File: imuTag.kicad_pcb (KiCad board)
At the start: 4 copper layers, 30 x 30 mm, 36 parts, among them J1 Conn_ARM_SWD_TagConnect_TC203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, U1 E73-2G4M08S1C, U2 MX25R6435FZAIL0, U4 LSM6DSV16XTR, U5 LIS2MDLTR, Y2 Crystal

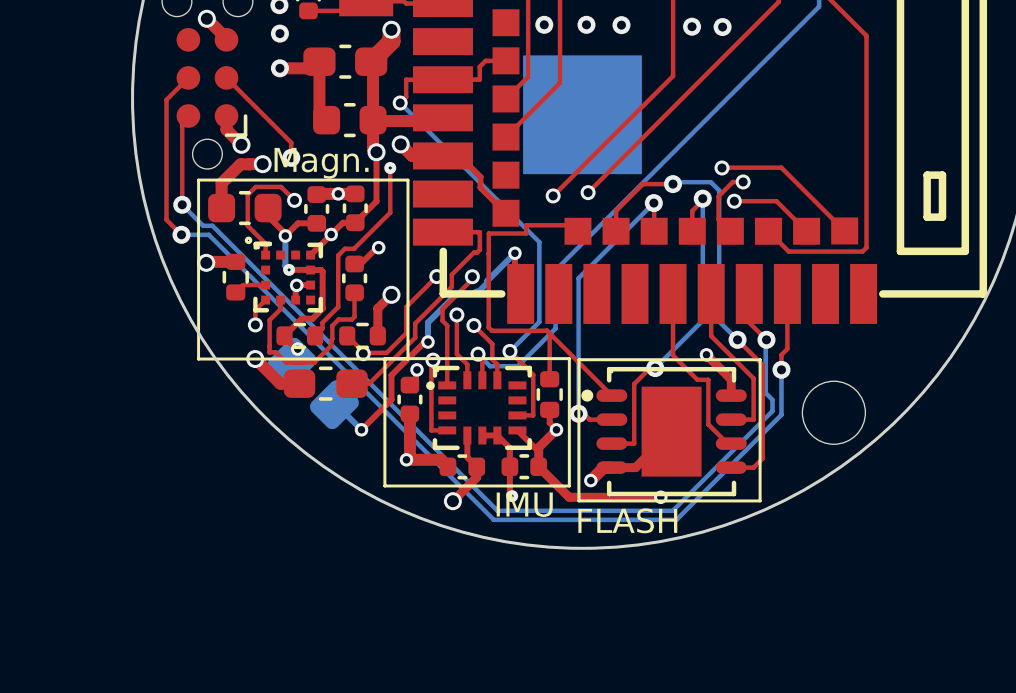
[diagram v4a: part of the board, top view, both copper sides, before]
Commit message: fix: minor wiring corrections under v1.2
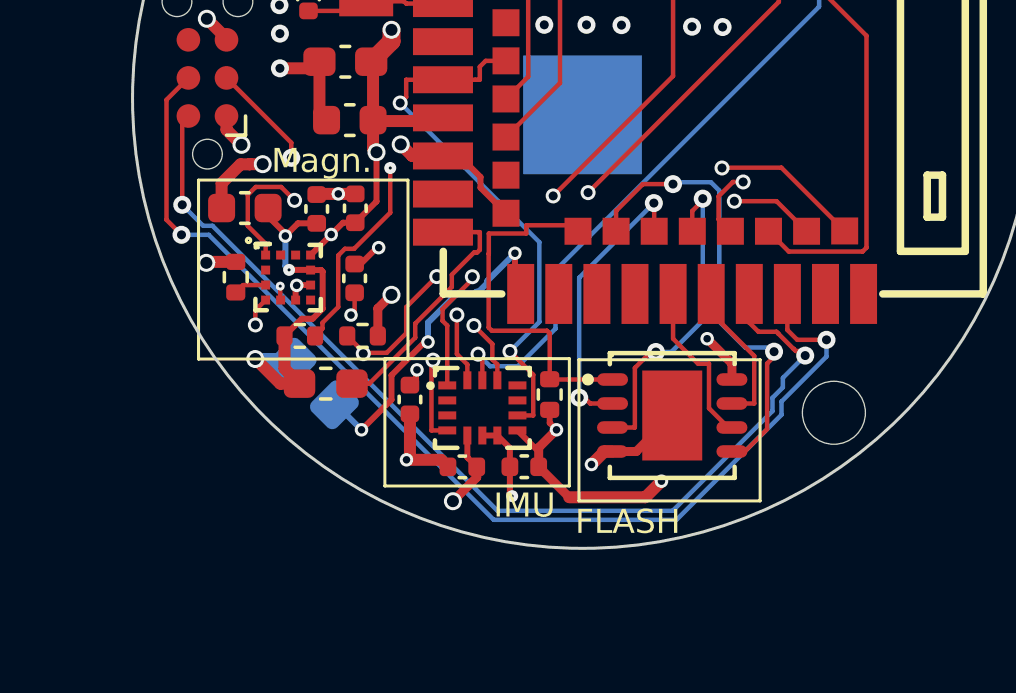
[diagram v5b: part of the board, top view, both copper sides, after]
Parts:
- moved U2 0.54 mm to (120.9, 111.0)
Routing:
- net VCC: track 45.7 -> 48.3 mm, vias 19 -> 18
- net Net-(U5-C1): track 6.67 -> 4.06 mm, vias 0 -> 2
- net /SWDIO: track 33.5 -> 35.8 mm
- net /SWDCLK: track 35.2 -> 36.9 mm
- net /QSPI_CS: track 13.2 -> 12.2 mm
- net /QSPI_IO1: track 10.2 -> 9.65 mm
- net /QSPI_CLK: track 6.08 -> 5.55 mm
- net /QSPI_IO3: track 5.77 -> 5.24 mm

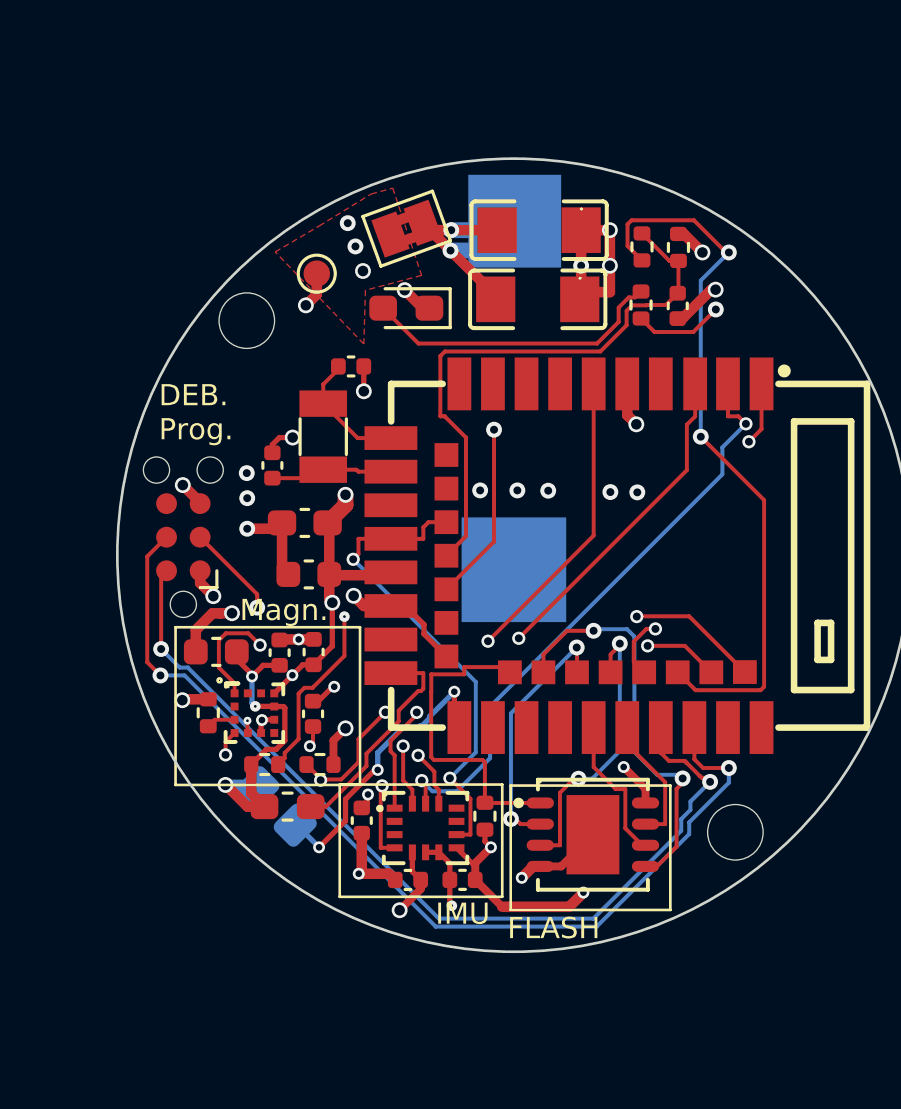
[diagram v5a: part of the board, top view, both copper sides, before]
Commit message: fix: wire unconnected pin and clear DRC exclusions
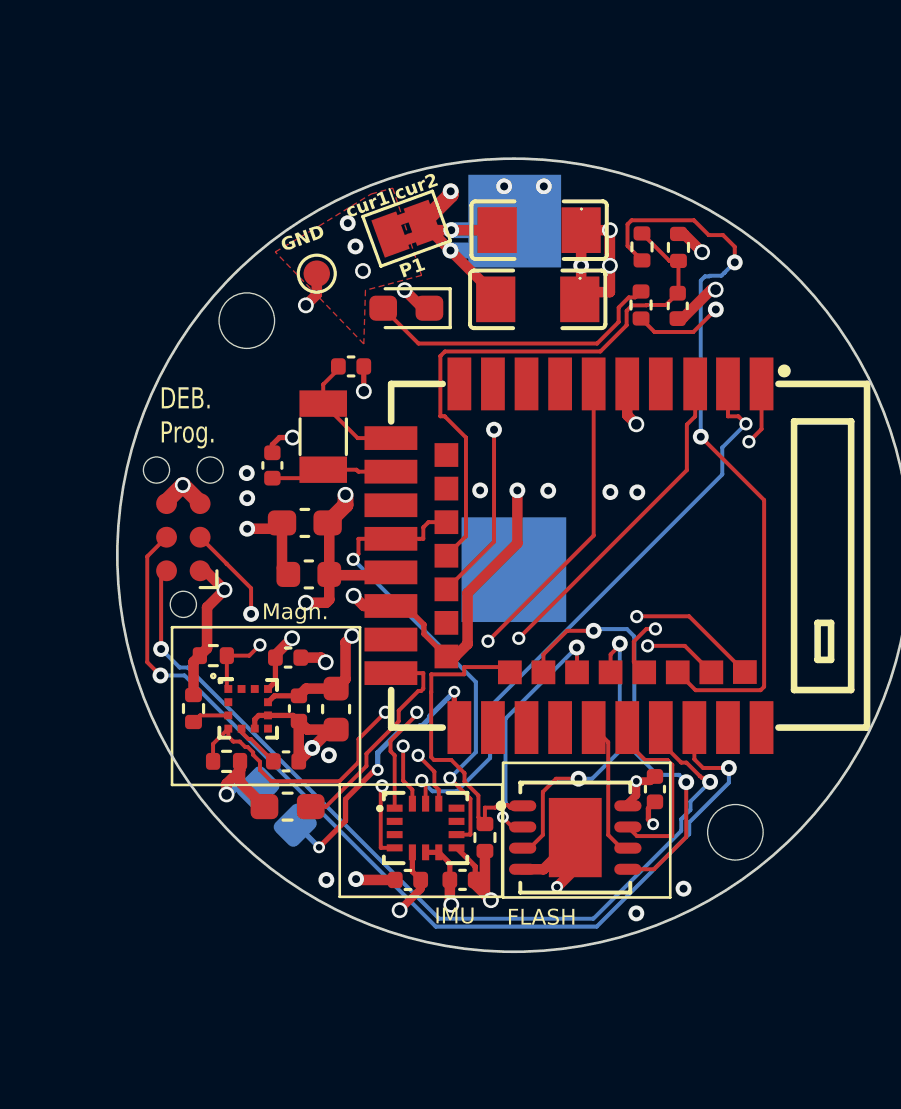
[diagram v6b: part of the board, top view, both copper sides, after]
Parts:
- moved C14 11.2 mm to (123.2, 109.3)
- moved C21 5.02 mm to (111.1, 106.3), turned to 90 degrees
- moved R16 4.56 mm to (106.5, 104.2)
- moved R18 3.54 mm to (107.0, 108.2)
- moved C19 2.24 mm to (109.7, 106.2), turned to 90 degrees
- moved C16 2.07 mm to (109.2, 108.2), turned to 180 degrees
- moved C17 0.99 mm to (109.3, 104.3), turned to 180 degrees
- moved R11 0.81 mm to (116.8, 111.1)
- moved U2 0.68 mm to (120.2, 111.1)
- moved R15 0.58 mm to (105.8, 106.2)
- moved U5 0.29 mm to (107.8, 106.3)
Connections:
- J1 pad 6: unconnected-(J1-SWO-Pad6) -> GND
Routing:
- net VCC: track 48.3 -> 36.3 mm, vias 18 -> 13
- net GND: track 39.6 -> 51.2 mm, vias 26 -> 29
- net /SPI1_MOSI: track 34.7 -> 26.3 mm
- net /I2C0_SCL: track 30.6 -> 22.4 mm, vias 3 -> 2
- net /QSPI_IO3: track 5.24 -> 7.76 mm
- net Net-(U5-C1): track 4.06 -> 1.79 mm, vias 2 -> 0
- net /SWDIO: track 35.8 -> 33.7 mm
- net /VBAT: track 14.3 -> 15.9 mm, vias 2 -> 5
- net /QSPI_IO0: track 15.4 -> 16.2 mm
- net /GPIO_BAT_MEAS: track 27.5 -> 28.2 mm
- net /QSPI_IO2: track 10.9 -> 11.4 mm
- net /I2C0_SDA: track 24.7 -> 25.2 mm, vias 4 -> 2
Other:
- board text added: "Battery-Type: C2032"
- board text added: "Bauer Labs IMU-TAG-Mini: A-1.0"
- board text added: "GND"
- board text added: "P1"
- board text added: "P1 current cut P1 and apply Probe Measurement to cur1 and cur2 ext.Power Apply Power-Supply to Supply GND and P1"
- board text added: "Prog. Interface GND GND SWDCLK RESET SWDIO VCC"
- board text added: "cur1|cur2"
- board text removed: "Bauer Labs IMU-TAG: A-1.0"
- board text removed: "C2032"

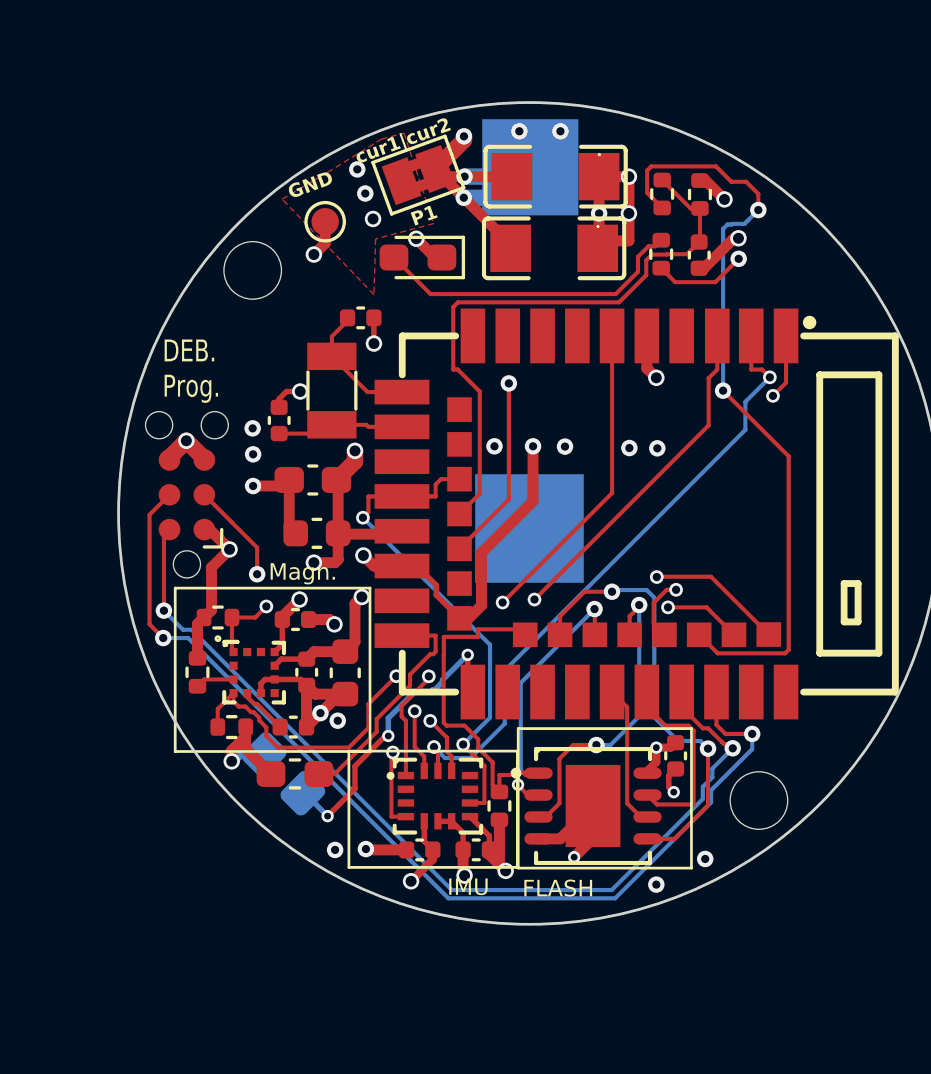
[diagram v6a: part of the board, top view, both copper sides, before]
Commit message: feat: optimize LIS2MDL layout for magnetic integrity
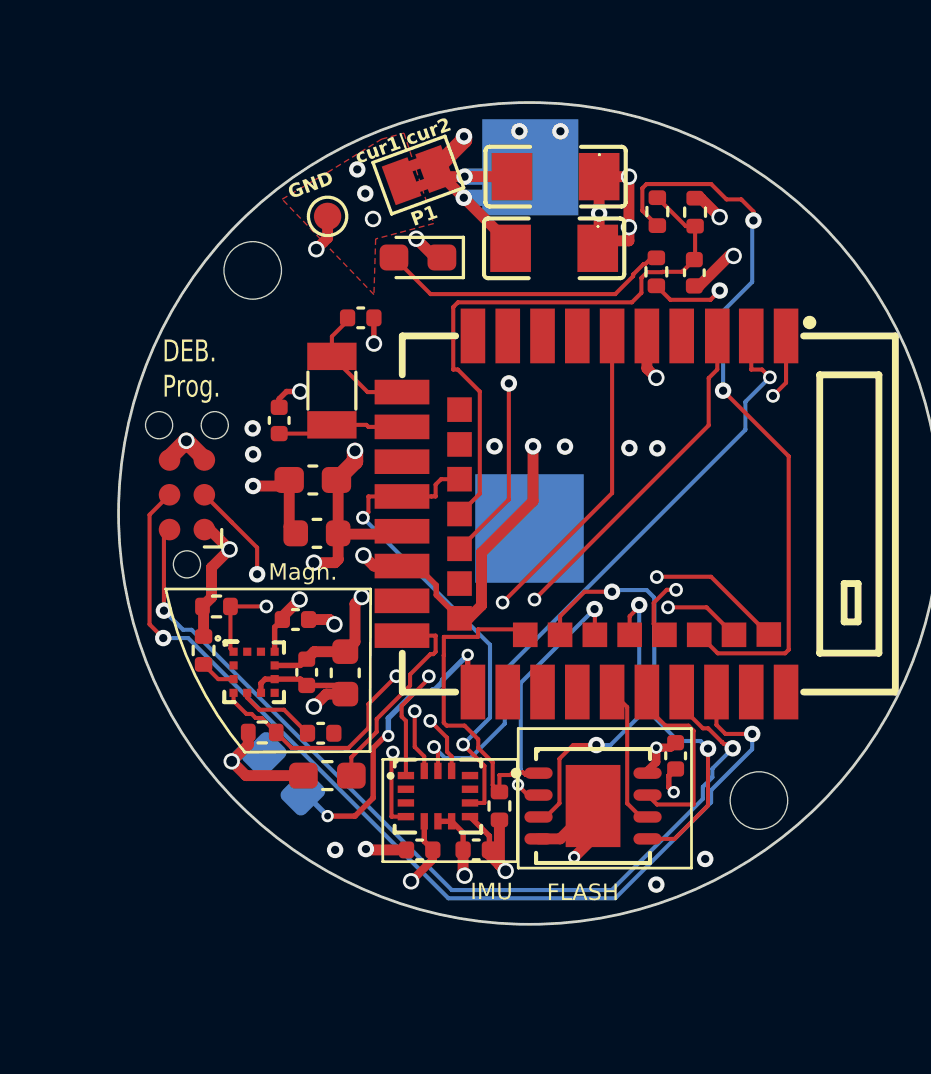
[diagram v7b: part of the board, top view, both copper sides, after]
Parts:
- moved L1 1.18 mm to (110.5, 110.0)
- moved R18 1.13 mm to (108.1, 108.4), turned to 0 degrees
- moved C16 1.02 mm to (110.2, 108.5)
- moved R15 0.83 mm to (106.0, 105.5)
- moved R3 0.67 mm to (122.5, 89.4)
- moved R2 0.67 mm to (123.9, 89.5)
- moved R5 0.67 mm to (122.5, 91.6)
- moved C1 0.67 mm to (123.9, 91.7)
- moved R16 0.41 mm to (106.4, 103.8)
- moved TP1 0.21 mm to (110.5, 89.6)
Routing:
- net GND: track 51.2 -> 49.1 mm, vias 29 -> 28
- net /LED1: track 20.4 -> 18.5 mm
- net /I2C0_SDA: track 25.2 -> 23.4 mm
- net Net-(U5-C1): track 1.79 -> 2.90 mm
- net /GPIO_BAT_MEAS: track 28.2 -> 27.2 mm
- net Net-(U1-DCH): track 8.44 -> 7.67 mm
- net Net-(D2-A): track 11.4 -> 10.7 mm
- net /RESET: track 26.4 -> 26.9 mm

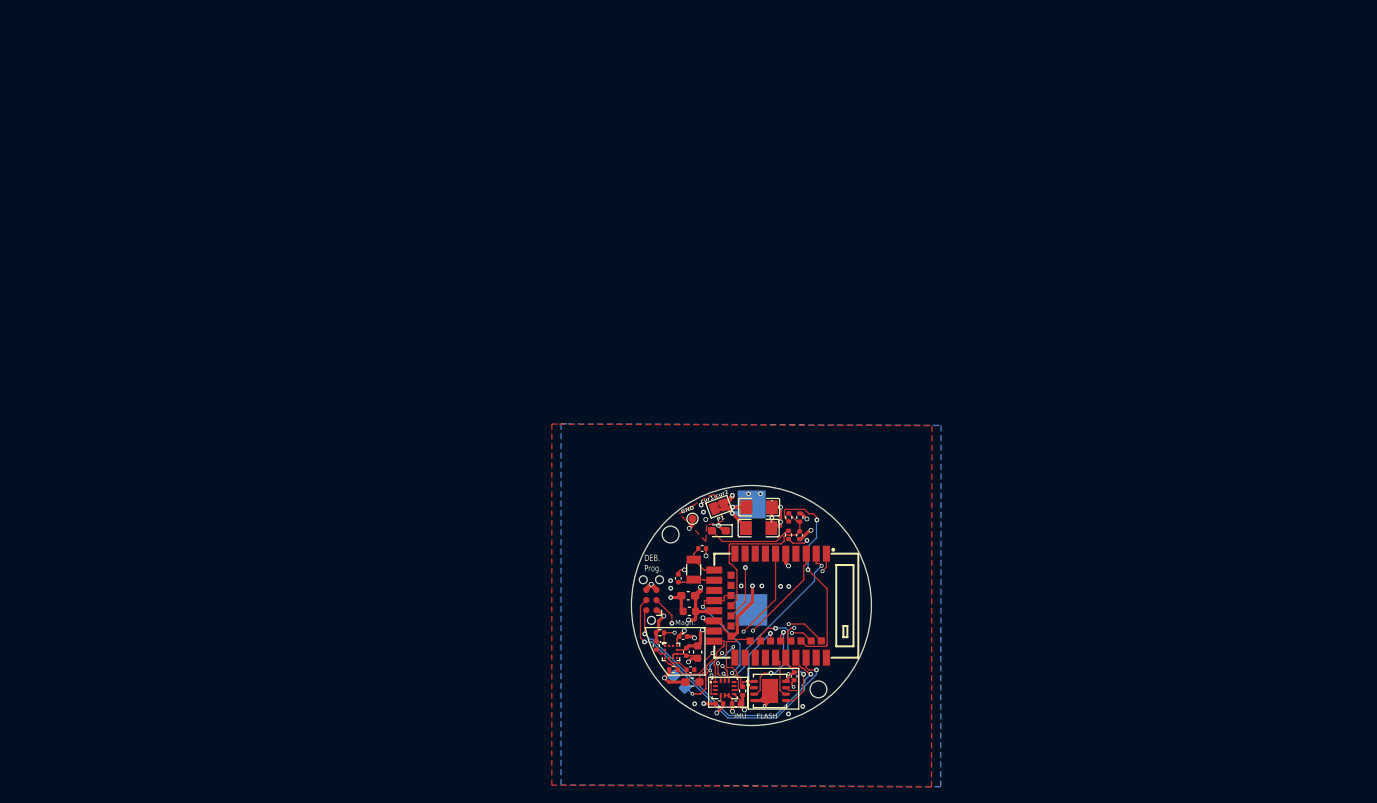
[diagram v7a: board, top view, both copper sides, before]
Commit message: feat: add NFC antenna support via E73-2G4M08S1C
- Add NFC matching network (ESD protection, 100pF tuning caps)
- Add hybrid antenna connector (JST SH 1.0mm + hand-solder test pads)
- Add 4-layer keepout zones around NFC traces and antenna feed
- Route and length-balance NFC1/NFC2 traces
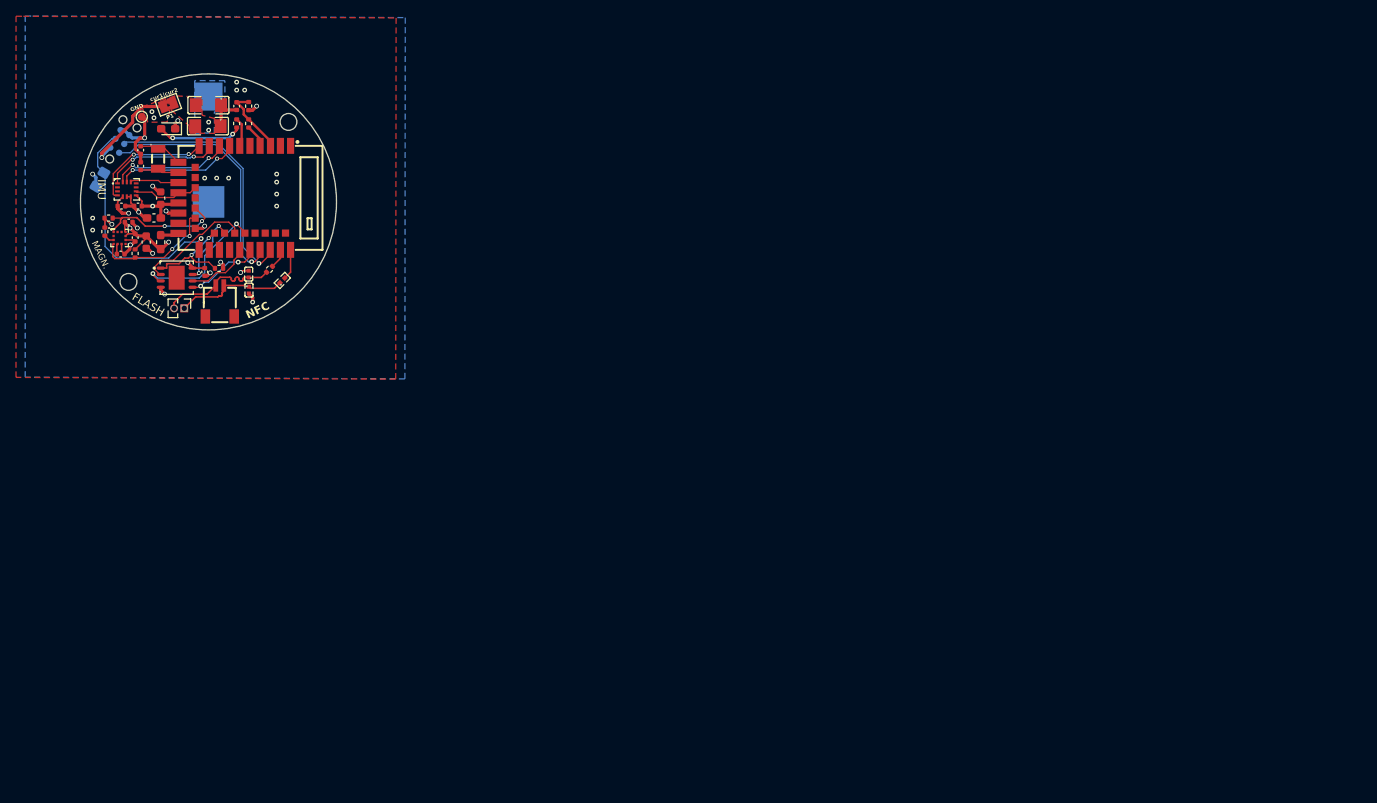
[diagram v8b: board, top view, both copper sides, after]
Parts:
- removed Y2: Crystal, Crystal:Crystal_SMD_3215-2Pin_3.2x1.5mm
- added C10: CC0402GRNPO9BN560, EasyEDA:C0402, F.Cu at (55.1, 61.0)
- added C9: CC0402GRNPO9BN560, EasyEDA:C0402, F.Cu at (55.0, 59.0)
- added CN1: SM02B-SRSS-TB, EasyEDA:CONN-SMD_2P-P1.00_SM02B-SRSS-TB-LF-SN, F.Cu at (51.4, 62.4)
- added J2: Conn_01x02_Pin, Connector_PinHeader_1.27mm:PinHeader_1x02_P1.27mm_Vertical, F.Cu at (47.0, 63.3)
- added R4: 0402WGF0000TCE, Resistor_SMD:R_0402_1005Metric, F.Cu at (57.6, 58.4)
- added R6: 0402WGF0000TCE, EasyEDA:R0402, F.Cu at (59.2, 59.8)
- added X1: Q13FC1350000400, EasyEDA:FC-135R_L3.2-W1.5, F.Cu at (43.7, 44.6)
- J1: moved to B.Cu
- moved H2 104.8 mm to (32.0, 53.5), turned to 0 degrees
- moved U4 97.3 mm to (39.8, 48.4)
- moved C20 97.2 mm to (39.1, 50.5), turned to 0 degrees
- moved C18 97.2 mm to (41.2, 50.5)
- moved H1 97.1 mm to (60.0, 40.0)
- moved R1 95.8 mm to (36.4, 47.2), turned to 60 degrees
- moved U2 90.4 mm to (46.0, 59.5)
- moved C14 89.4 mm to (49.5, 58.8)
- moved C1 88.5 mm to (53.5, 38.0)
- moved C16 88.2 mm to (39.0, 56.5)
- moved J1 87.8 mm to (38.9, 42.4), turned to 60 degrees
- moved C17 86.5 mm to (40.0, 52.5)
- moved L1 86.3 mm to (44.0, 55.0), turned to -90 degrees
- moved R16 86.2 mm to (37.5, 52.0)
- moved C19 86.2 mm to (40.8, 54.5)
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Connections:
- U1 pad 1: /SPI1_MOSI -> unconnected-(U1-P1.11-Pad1)
- U1 pad 10: unconnected-(U1-AI6-Pad10) -> /LSM6DSV16_INT1
- U1 pad 15: unconnected-(U1-AI3-Pad15) -> /LSM6DSV16_CS
- U1 pad 18: /BATTERY_PIN -> unconnected-(U1-AI2-Pad18)
- U1 pad 2: /SPI1_SCLK -> unconnected-(U1-P1.10-Pad2)
- U1 pad 20: /LED1 -> /I2C0_SCL
- U1 pad 22: unconnected-(U1-P0.07-Pad22) -> /I2C0_SDA
- U1 pad 3: /LSM6DSV16_CS -> /BATTERY_PIN
- U1 pad 30: /QSPI_IO0 -> /QSPI_IO3
- U1 pad 35: /QSPI_IO3 -> /QSPI_IO0
- U1 pad 36: /LSM6DSV16_INT1 -> unconnected-(U1-P1.00-Pad36)
- U1 pad 38: /GPIO_BAT_MEAS -> unconnected-(U1-P1.02-Pad38)
- U1 pad 4: unconnected-(U1-AI4-Pad4) -> /GPIO_BAT_MEAS
- U1 pad 40: /I2C0_SDA -> unconnected-(U1-P1.04-Pad40)
- U1 pad 41: unconnected-(U1-NF1-Pad41) -> /NFC1
- U1 pad 42: /I2C0_SCL -> unconnected-(U1-P1.06-Pad42)
- U1 pad 43: unconnected-(U1-NF2-Pad43) -> /NFC2
- U1 pad 6: /SPI1_MISO -> /LED1
- U1 pad 7: unconnected-(U1-AI0-Pad7) -> /SPI1_SCLK
- U1 pad 8: unconnected-(U1-AI5-Pad8) -> /SPI1_MOSI
- U1 pad 9: unconnected-(U1-AI7-Pad9) -> /SPI1_MISO
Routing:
- net /GPIO_BAT_MEAS: track 27.2 -> 2.88 mm, vias 2 -> 0
- net /VBAT: track 15.9 -> 0.00 mm, vias 5 -> 2
- net Net-(J2-Pin_2): track 0.00 -> 15.4 mm
- net /LED1: track 18.5 -> 3.93 mm, vias 2 -> 0
- net /LSM6DSV16_CS: track 20.5 -> 6.14 mm, vias 2 -> 0
- net Net-(J2-Pin_1): track 0.00 -> 14.2 mm
- net /BATTERY_PIN: track 21.2 -> 8.71 mm
- net /SPI1_MOSI: track 26.3 -> 15.2 mm
- net /LSM6DSV16_INT2: track 18.3 -> 8.20 mm, vias 2 -> 0
- net VCC: track 36.0 -> 45.2 mm, vias 13 -> 12
- net /I2C0_SDA: track 23.4 -> 15.4 mm
- net /SPI1_SCLK: track 22.9 -> 15.5 mm
- net /QSPI_IO0: track 16.2 -> 9.62 mm
- net /QSPI_IO2: track 11.4 -> 17.8 mm
- net /I2C0_SCL: track 22.7 -> 16.4 mm
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- added copper zone on B.Cu, net /VBAT
- added copper zone on F.Cu, net /VBAT
- removed copper zone on In2.Cu, net /VBAT
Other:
- board size 30 x 30 mm -> 32 x 32 mm
- board text added: "Battery-Type: CR2032"
- board text added: "Bauer Labs Motion-Tag-Mini: A-1.0"
- board text added: "MAGN."
- board text added: "NFC"
- board text added: "Prog."
- board text added: "Pullup option RESET (P0.18)"
- board text removed: "Battery-Type: C2032"
- board text removed: "Bauer Labs IMU-TAG-Mini: A-1.0"
- board text removed: "DEB. Prog."
- board text removed: "Magn."
